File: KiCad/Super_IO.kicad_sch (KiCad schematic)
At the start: 19 parts, among them J13 Serial2, J14 Floppy, J15 Primary IDE, J4 Serial1, J5 Parallel, U12 FDC37C655GT, U13 GD75232N, U14 GD75232N, U67 74F245, U68 74F245, U69 74F541, Y2 24MHz

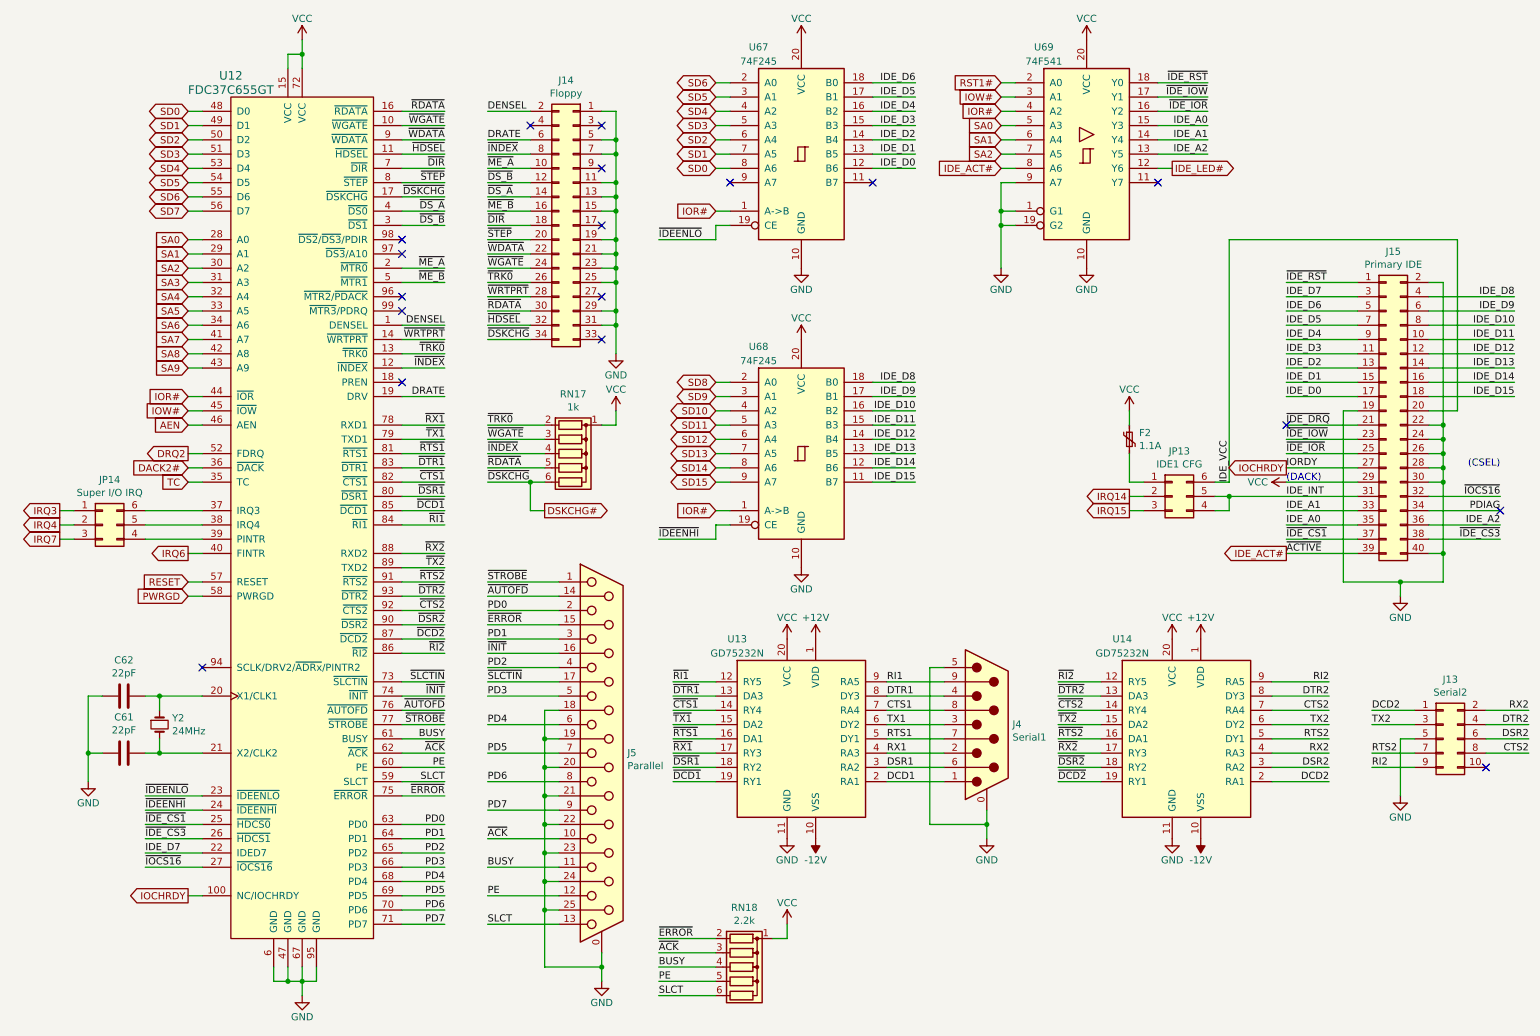
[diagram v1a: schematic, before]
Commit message: Version 0.4: Update chipset connection
Signed-off-by: Sergey Kiselev <skiselev@gmail.com>
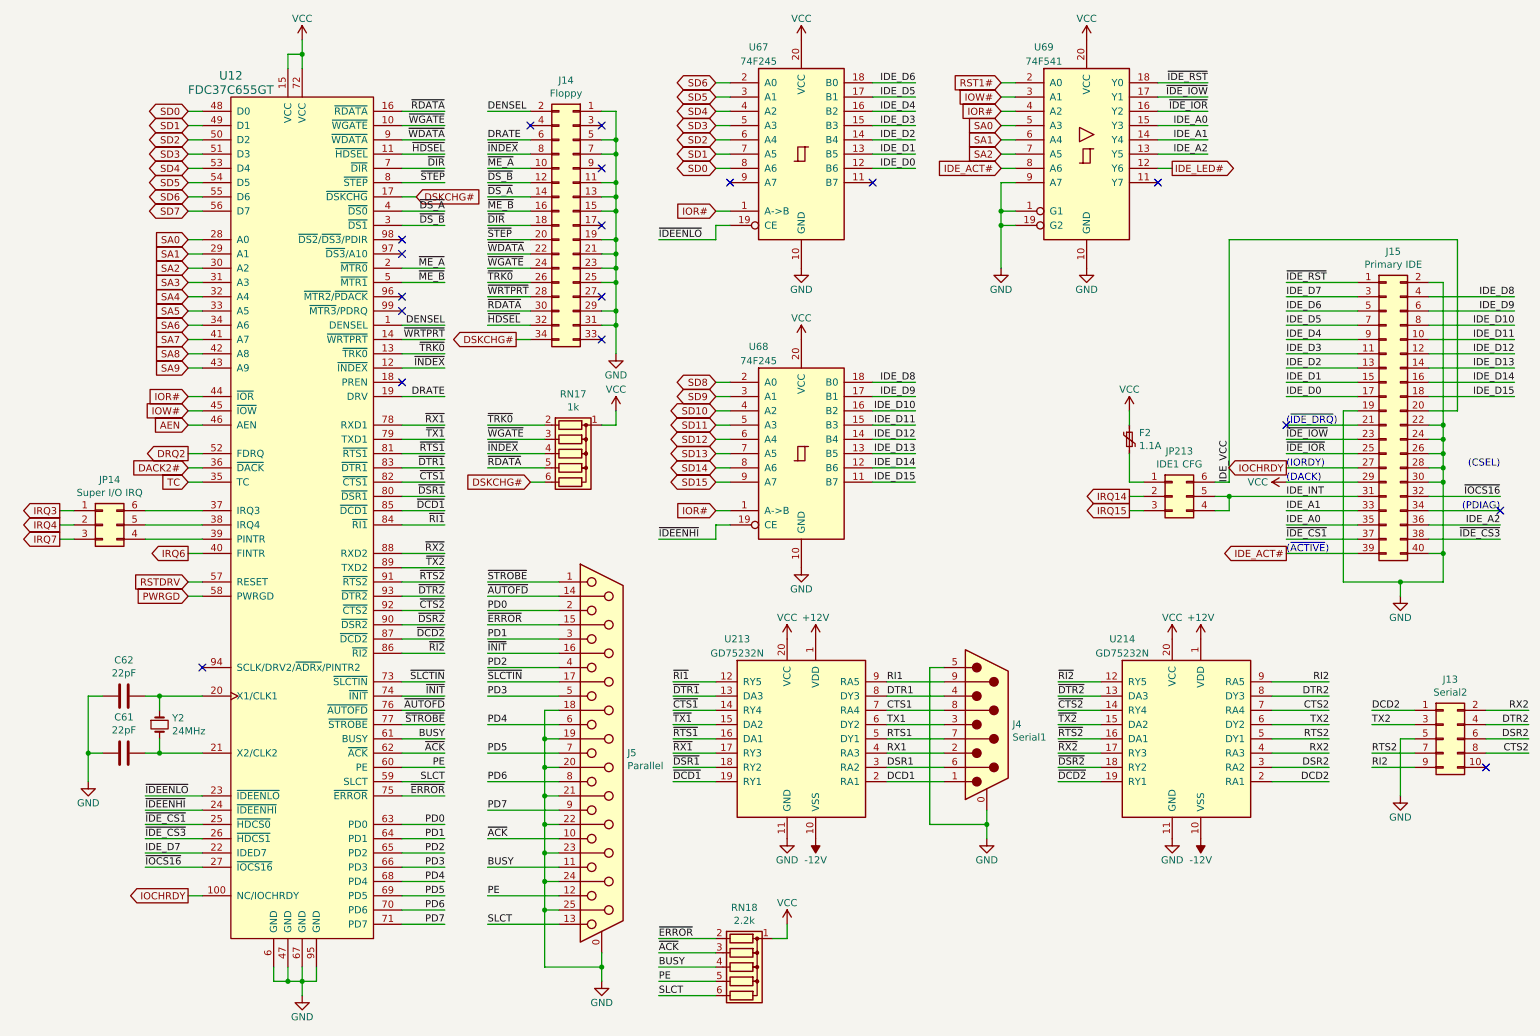
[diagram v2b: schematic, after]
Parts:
- C61, C62: footprint (none) -> Capacitor_SMD:C_0603_1608Metric_Pad1.08x0.95mm_HandSolder
- F2: footprint (none) -> Fuse:Fuse_Littelfuse_395Series
- J13: footprint (none) -> Connector_PinHeader_2.54mm:PinHeader_2x05_P2.54mm_Vertical
- J14: footprint (none) -> My_Components:Conn_Pin_Header_17x2_2.54mm_Shrouded
- J15: footprint (none) -> My_Components:Conn_Pin_Header_20x2_2.54mm
- J4: footprint (none) -> My_Components:Conn_Dsub_DE9M
- J5: footprint (none) -> My_Components:Conn_Dsub_DB25F
- JP14: footprint (none) -> My_Components:Conn_Pin_Header_2x3_2.54mm
- JP213: renamed from JP13; footprint (none) -> My_Components:Conn_Pin_Header_2x3_2.54mm
- U12: footprint (none) -> My_Components:IC_PQFP-100_14x20mm_P0.65mm_Hand_Soldering
- U213: renamed from U13; footprint Package_DIP:DIP-20_W7.62mm -> My_Components:IC_DIP20_300
- U214: renamed from U14; footprint Package_DIP:DIP-20_W7.62mm -> My_Components:IC_DIP20_300
- U67, U68, U69: footprint (none) -> My_Components:IC_DIP20_300
- Y2: footprint (none) -> My_Components:Crystal_HC-49U_Vert
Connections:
- net PDIAG: no longer names the net of J15.34 (Pin_34)
- net RESET renamed RSTDRV
- net ~{IDE_DRQ}: no longer names the net of J15.21 (Pin_21)
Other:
- note added: "(IORDY)"
- note added: "(PDIAG)"
- note added: "(~{ACTIVE})"
- note added: "(~{IDE_DRQ})"

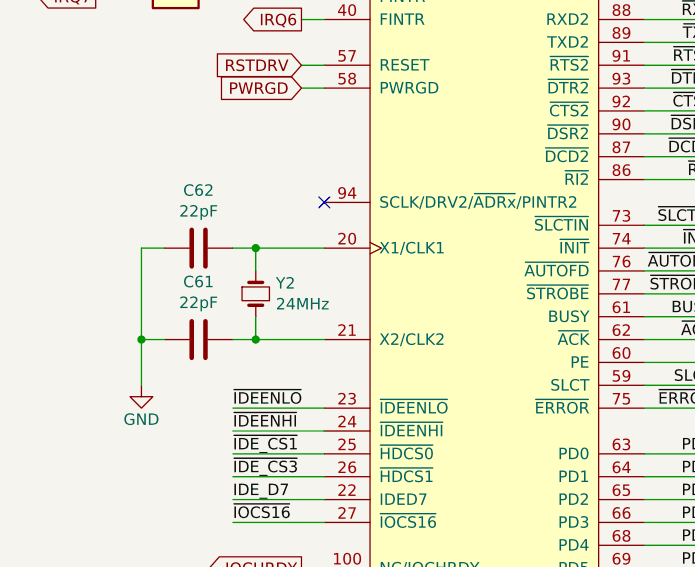
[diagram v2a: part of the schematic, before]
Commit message: More schematic updates. Remove old KiCad files
Signed-off-by: Sergey Kiselev <skiselev@gmail.com>
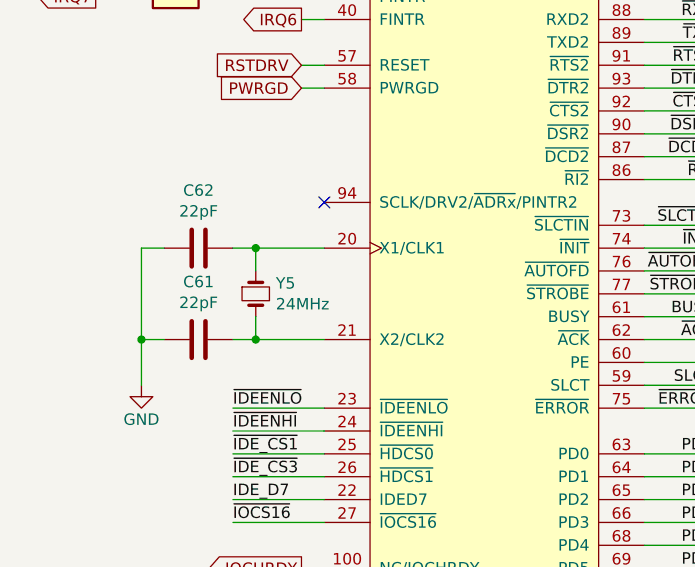
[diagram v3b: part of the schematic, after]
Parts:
- renumbered Y2 to Y5
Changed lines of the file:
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@@
   (symbol (lib_id "Device:Crystal_Small") (at 38.1 139.7 270) (unit 1)
     (in_bom yes) (on_board yes)
-    (property "Reference" "Y2" (id 0) (at 40.3352 138.5316 90)
+    (property "Reference" "Y5" (id 0) (at 40.3352 138.5316 90)
       (effects (font (size 1.27 1.27)) (justify left))
     )
